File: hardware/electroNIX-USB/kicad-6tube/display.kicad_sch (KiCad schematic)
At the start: 87 parts, among them Q10 MMBTA42, Q11 MMBTA92, Q12 MMBTA42, Q13 MMBTA92, Q14 MMBTA42, Q15 MMBTA92, Q16 MMBTA42, Q17 MMBTA42, Q18 MMBTA42, Q19 MMBTA42, Q20 MMBTA42, Q21 MMBTA42, Q22 MMBTA42, Q23 MMBTA42, Q24 MMBTA42, Q25 MMBTA42, Q26 MMBTA42, Q27 MMBTA42, Q4 MMBTA42, Q5 MMBTA92, Q6 MMBTA42, Q7 MMBTA92, Q8 MMBTA42, Q9 MMBTA92

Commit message: electroNIX-USB: apply RFT Z573M data sheet, add tube footprint
The data book confirms the pinout already in the symbol. The tube is
side-view (not top-view), with 13 flying leads on a 9.53 mm circle and
wire 7 at the front. New footprint electronix:Nixie_RFT_Z573M (top
view, wire 7 toward the front edge) is assigned to the tubes.

Tube current: Ik is 1.5-2.5 mA continuous, 12 mA pulse. PCB-036's 10k
anode resistors averaged only ~0.75 mA per tube when multiplexed. Anode
resistors are now 5k6 (4 tubes) and 3k9 (6 tubes), cathode base
resistors 6k8. To carry the extra HV power, the ladder caps go to
2.2 uF and the 6-tube build uses a 22 uH inductor.

Co-Authored-By: Claude Opus 5.5 <noreply@anthropic.com>
Claude-Session: https://claude.ai/code/session_01AFMfevKEKDGbci8uJGhf4W
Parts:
- N1, N2, N3, N4, N5, N6: footprint (none) -> electronix:Nixie_RFT_Z573M
- R16, R20, R24, R28, R32, R36: value 10k -> 3k9
- R37, R38, R39, R40, R41, R42, R43, R44, R45, R46: value 15k -> 6k8
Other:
- note added: "Pin 4 = internal connection (leave open). Pin 10 = decimal point (unused). Pinout per RFT data book (frank.pocnet.net/sheets/084/z/Z573M.pdf)."
- note added: "Tubes (RFT Z573M side-view, 13 flying leads on 9.53 mm circle, wire 7 at front)"
- note added: "W_n high -> tube n anode at +170V through 3k9: ~7.7 mA peak at 170 V, ~1.3 mA average per tube (Z573M: 1.5-2.5 mA cont., 12 mA pulse). Peak current follows (V_HV - 140 V): keep the firmware HV setpoint <= 180 V. W_5/W_6 = IO12/IO15 (seconds tubes)."
- note removed: "Pin 4 = internal connection (leave open). Pin 10 = PR sign (unused). Pinout from tube-tester.com Z573M page; check against a real tube before layout."
- note removed: "Tubes (RFT Z573M, B13D base, pin 7 at front)"
- note removed: "W_n high -> tube n anode at +170V through 10k. Anode current ~2 mA peak. W_5/W_6 = IO12/IO15 (seconds tubes)."
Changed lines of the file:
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@@
       (justify left top))
 )
-  (text "W_n high -> tube n anode at +170V through 10k. Anode current ~2 mA peak.  W_5/W_6 = IO12/IO15 (seconds tubes)."
-    (at 25 98 0)
+  (text "W_n high -> tube n anode at +170V through 3k9: ~7.7 mA peak at 170 V, ~1.3 mA average per tube (Z573M: 1.5-2.5 mA cont., 12 mA pulse).\nPeak current follows (V_HV - 140 V): keep the firmware HV setpoint <= 180 V.  W_5/W_6 = IO12/IO15 (seconds tubes)."
+    (at 25 95 0)
     (effects
       (font
@@
       (type none))
 )
-  (text "Tubes (RFT Z573M, B13D base, pin 7 at front)"
+  (text "Tubes (RFT Z573M side-view, 13 flying leads on 9.53 mm circle, wire 7 at front)"
     (at 21.27 116.27 0)
     (effects
@@
       (justify left top))
 )
-  (text "Pin 4 = internal connection (leave open). Pin 10 = PR sign (unused).\nPinout from tube-tester.com Z573M page; check against a real tube before layout."
+  (text "Pin 4 = internal connection (leave open). Pin 10 = decimal point (unused).\nPinout per RFT data book (frank.pocnet.net/sheets/084/z/Z573M.pdf)."
     (at 25 195 0)
     (effects
@@
           (size 1.27 1.27))
         (justify left)))
-    (property "Value" "10k"
+    (property "Value" "3k9"
       (at 60.96 77.47 0)
       (effects
@@
           (size 1.27 1.27))
         (justify left)))
-    (property "Value" "10k"
+    (property "Value" "3k9"
       (at 123.19 77.47 0)
       (effects
@@
           (size 1.27 1.27))
         (justify left)))
-    (property "Value" "10k"
+    (property "Value" "3k9"
       (at 185.42 77.47 0)
       (effects
@@
           (size 1.27 1.27))
         (justify left)))
-    (property "Value" "10k"
+    (property "Value" "3k9"
       (at 247.65 77.47 0)
       (effects
@@
           (size 1.27 1.27))
         (justify left)))
-    (property "Value" "10k"
+    (property "Value" "3k9"
       (at 309.88 77.47 0)
       (effects
@@
           (size 1.27 1.27))
         (justify left)))
-    (property "Value" "10k"
+    (property "Value" "3k9"
       (at 370.84 77.47 0)
       (effects
@@
           (size 1.27 1.27))
         (justify left)))
-    (property "Footprint" ""
+    (property "Footprint" "electronix:Nixie_RFT_Z573M"
       (at 59.69 160.02 0)
       (effects
@@
           (size 1.27 1.27))
         (justify left)))
-    (property "Footprint" ""
+    (property "Footprint" "electronix:Nixie_RFT_Z573M"
       (at 121.92 160.02 0)
       (effects
@@
           (size 1.27 1.27))
         (justify left)))
-    (property "Footprint" ""
+    (property "Footprint" "electronix:Nixie_RFT_Z573M"
       (at 184.15 160.02 0)
       (effects
@@
           (size 1.27 1.27))
         (justify left)))
-    (property "Footprint" ""
+    (property "Footprint" "electronix:Nixie_RFT_Z573M"
       (at 246.38 160.02 0)
       (effects
@@
           (size 1.27 1.27))
         (justify left)))
-    (property "Footprint" ""
+    (property "Footprint" "electronix:Nixie_RFT_Z573M"
       (at 308.61 160.02 0)
       (effects
@@
           (size 1.27 1.27))
         (justify left)))
-    (property "Footprint" ""
+    (property "Footprint" "electronix:Nixie_RFT_Z573M"
       (at 369.57 160.02 0)
       (effects
@@
         (font
           (size 1.27 1.27))))
-    (property "Value" "15k"
+    (property "Value" "6k8"
       (at 35.56 273.05 90)
       (effects
@@
         (font
           (size 1.27 1.27))))
-    (property "Value" "15k"
+    (property "Value" "6k8"
       (at 72.39 273.05 90)
       (effects
@@
         (font
           (size 1.27 1.27))))
-    (property "Value" "15k"
+    (property "Value" "6k8"
       (at 107.95 273.05 90)
       (effects
@@
         (font
           (size 1.27 1.27))))
-    (property "Value" "15k"
+    (property "Value" "6k8"
       (at 143.51 273.05 90)
       (effects
@@
         (font
           (size 1.27 1.27))))
-    (property "Value" "15k"
+    (property "Value" "6k8"
       (at 180.34 273.05 90)
       (effects
@@
         (font
           (size 1.27 1.27))))
-    (property "Value" "15k"
+    (property "Value" "6k8"
       (at 215.9 273.05 90)
       (effects
@@
         (font
           (size 1.27 1.27))))
-    (property "Value" "15k"
+    (property "Value" "6k8"
       (at 252.73 273.05 90)
       (effects
@@
         (font
           (size 1.27 1.27))))
-    (property "Value" "15k"
+    (property "Value" "6k8"
       (at 288.29 273.05 90)
       (effects
@@
         (font
           (size 1.27 1.27))))
-    (property "Value" "15k"
+    (property "Value" "6k8"
       (at 323.85 273.05 90)
       (effects
@@
         (font
           (size 1.27 1.27))))
-    (property "Value" "15k"
+    (property "Value" "6k8"
       (at 360.68 273.05 90)
       (effects

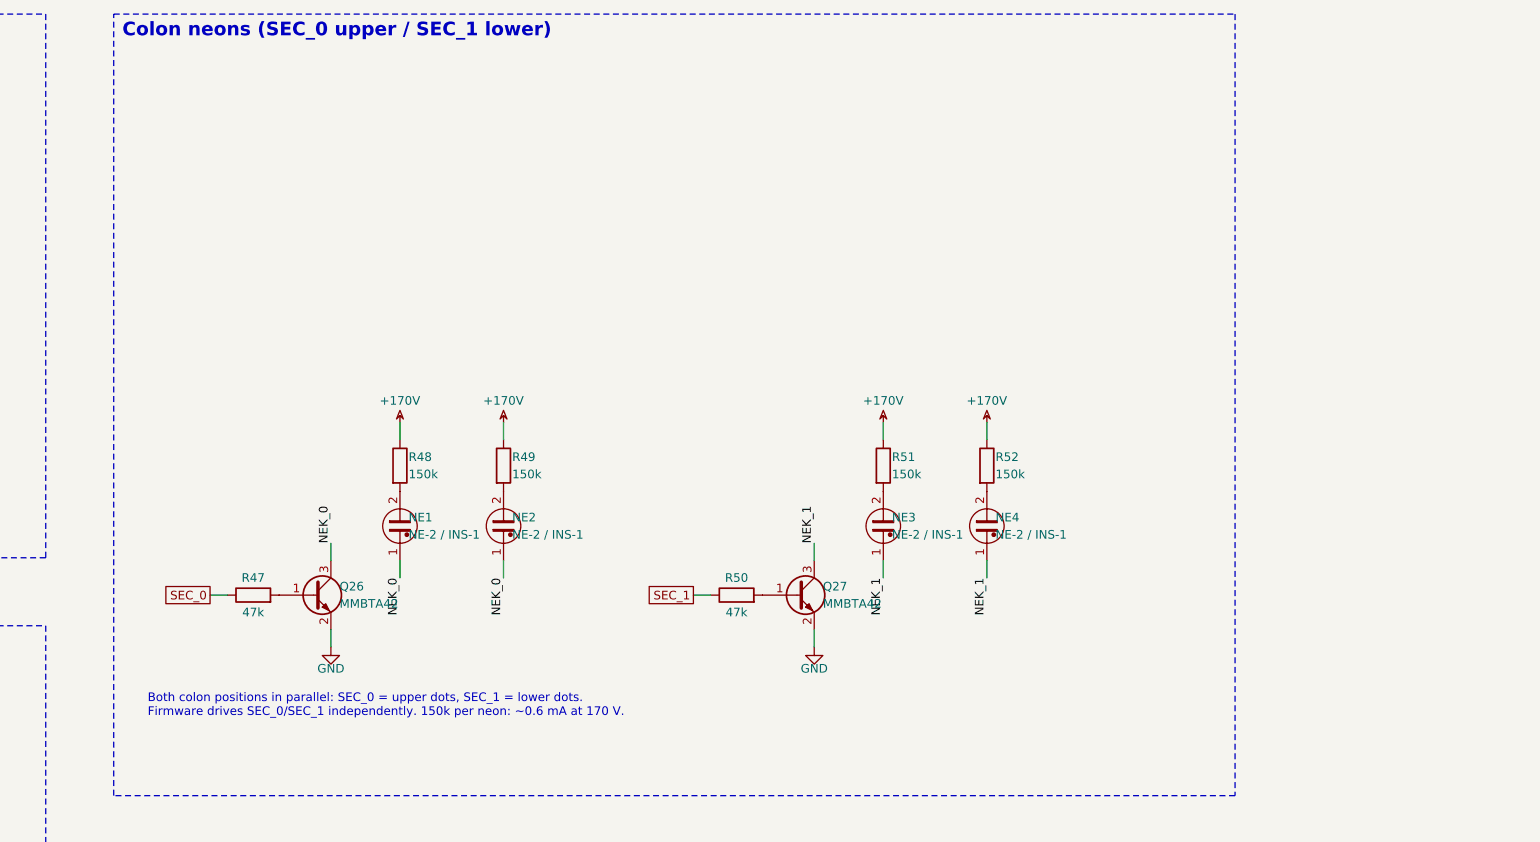
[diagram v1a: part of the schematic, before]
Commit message: electroNIX-USB: socket-adapter footprint, 0.1in neons, 4-tube PCB placement (WIP)
- Z573M socket pins on the electroNIX-2 adapter's 12.6 mm outer ring
  (default footprint), and the direct 9.53 mm footprint resized for the
  1.48 mm socket pins
- Neon_P2.54mm footprint. 6 tubes: HH:MM colon on SEC_0, MM:SS on SEC_1
- SET is a right-angle tact switch; RESET/BOOT use KMR2; low-voltage anode
  resistors moved to 0805
- source/pcb.py: builds the board from the netlist (placement, net
  classes, ESP32 antenna keepout, Freerouting, GND pours, DRC);
  source/fab.sh: fab outputs
- 4-tube board placed (102 x 66 mm, the original kit size), not yet routed

Co-Authored-By: Claude Opus 5.5 <noreply@anthropic.com>
Claude-Session: https://claude.ai/code/session_01AFMfevKEKDGbci8uJGhf4W
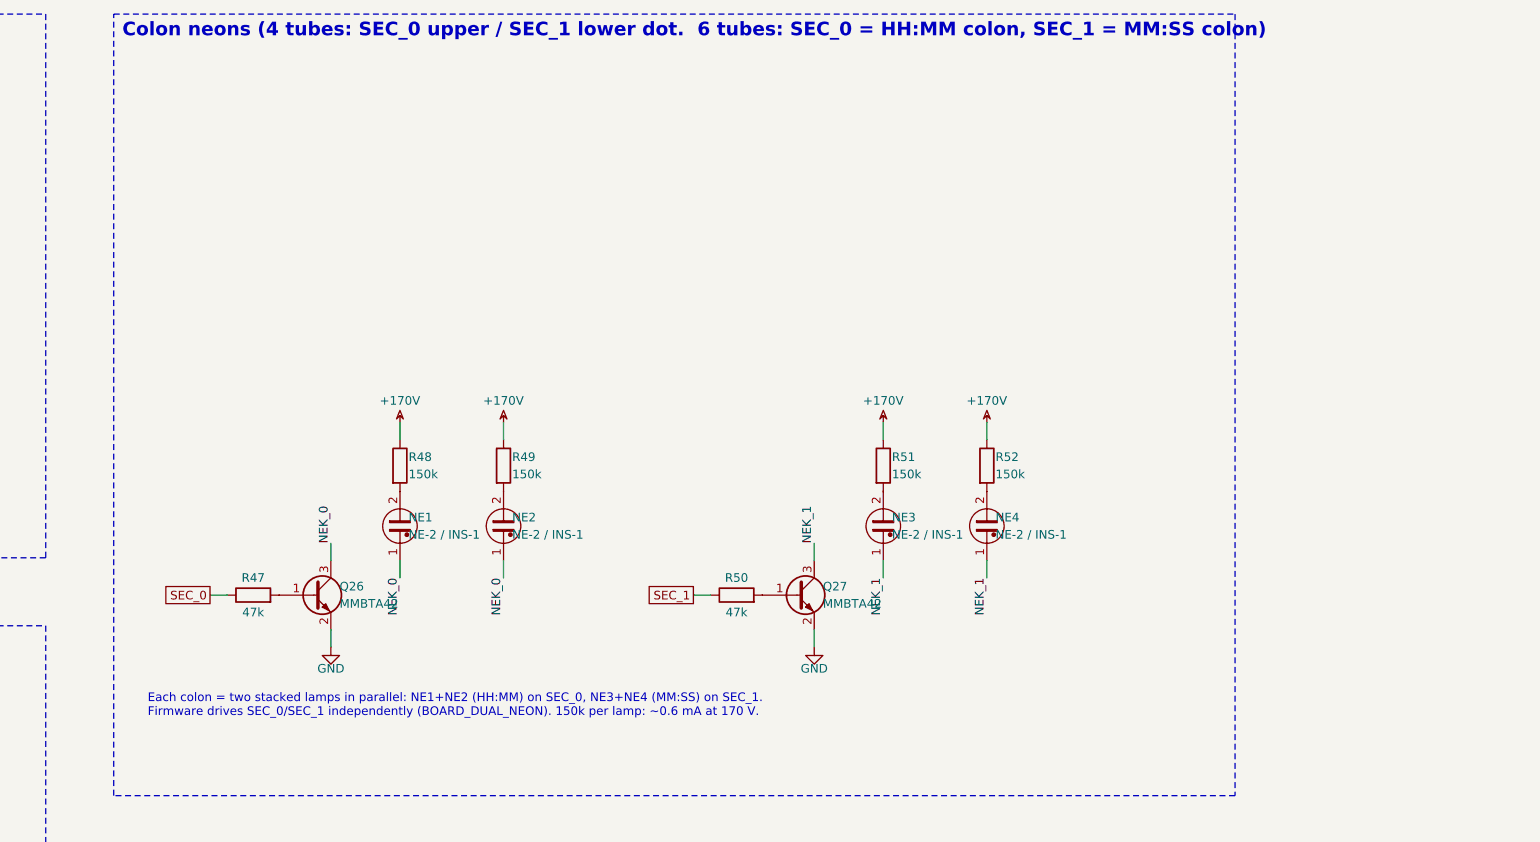
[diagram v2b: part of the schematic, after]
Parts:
- N1, N2, N3, N4, N5, N6: footprint electronix:Nixie_RFT_Z573M -> electronix:Nixie_RFT_Z573M_Adapter
- NE1, NE2, NE3, NE4: footprint (none) -> electronix:Neon_P2.54mm
- R15, R16, R19, R20, R23, R24, R27, R28, R31, R32, R35, R36: footprint Resistor_SMD:R_1206_3216Metric -> Resistor_SMD:R_0805_2012Metric
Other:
- note added: "Colon neons (4 tubes: SEC_0 upper / SEC_1 lower dot. 6 tubes: SEC_0 = HH:MM colon, SEC_1 = MM:SS colon)"
- note added: "Each colon = two stacked lamps in parallel: NE1+NE2 (HH:MM) on SEC_0, NE3+NE4 (MM:SS) on SEC_1. Firmware drives SEC_0/SEC_1 independently (BOARD_DUAL_NEON). 150k per lamp: ~0.6 mA at 170 V."
- note removed: "Both colon positions in parallel: SEC_0 = upper dots, SEC_1 = lower dots. Firmware drives SEC_0/SEC_1 independently. 150k per neon: ~0.6 mA at 170 V."
- note removed: "Colon neons (SEC_0 upper / SEC_1 lower)"
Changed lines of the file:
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@@
       (type none))
 )
-  (text "Colon neons (SEC_0 upper / SEC_1 lower)"
+  (text "Colon neons (4 tubes: SEC_0 upper / SEC_1 lower dot.  6 tubes: SEC_0 = HH:MM colon, SEC_1 = MM:SS colon)"
     (at 411.27 26.27 0)
     (effects
@@
       (justify left top))
 )
-  (text "Both colon positions in parallel: SEC_0 = upper dots, SEC_1 = lower dots.\nFirmware drives SEC_0/SEC_1 independently. 150k per neon: ~0.6 mA at 170 V."
+  (text "Each colon = two stacked lamps in parallel: NE1+NE2 (HH:MM) on SEC_0, NE3+NE4 (MM:SS) on SEC_1.\nFirmware drives SEC_0/SEC_1 independently (BOARD_DUAL_NEON). 150k per lamp: ~0.6 mA at 170 V."
     (at 415 125 0)
     (effects
@@
           (size 1.27 1.27))
         (justify left)))
-    (property "Footprint" "Resistor_SMD:R_1206_3216Metric"
+    (property "Footprint" "Resistor_SMD:R_0805_2012Metric"
       (at 52.07 63.5 0)
       (effects
@@
           (size 1.27 1.27))
         (justify left)))
-    (property "Footprint" "Resistor_SMD:R_1206_3216Metric"
+    (property "Footprint" "Resistor_SMD:R_0805_2012Metric"
       (at 59.69 76.2 0)
       (effects
@@
           (size 1.27 1.27))
         (justify left)))
-    (property "Footprint" "Resistor_SMD:R_1206_3216Metric"
+    (property "Footprint" "Resistor_SMD:R_0805_2012Metric"
       (at 114.3 63.5 0)
       (effects
@@
           (size 1.27 1.27))
         (justify left)))
-    (property "Footprint" "Resistor_SMD:R_1206_3216Metric"
+    (property "Footprint" "Resistor_SMD:R_0805_2012Metric"
       (at 121.92 76.2 0)
       (effects
@@
           (size 1.27 1.27))
         (justify left)))
-    (property "Footprint" "Resistor_SMD:R_1206_3216Metric"
+    (property "Footprint" "Resistor_SMD:R_0805_2012Metric"
       (at 176.53 63.5 0)
       (effects
@@
           (size 1.27 1.27))
         (justify left)))
-    (property "Footprint" "Resistor_SMD:R_1206_3216Metric"
+    (property "Footprint" "Resistor_SMD:R_0805_2012Metric"
       (at 184.15 76.2 0)
       (effects
@@
           (size 1.27 1.27))
         (justify left)))
-    (property "Footprint" "Resistor_SMD:R_1206_3216Metric"
+    (property "Footprint" "Resistor_SMD:R_0805_2012Metric"
       (at 238.76 63.5 0)
       (effects
@@
           (size 1.27 1.27))
         (justify left)))
-    (property "Footprint" "Resistor_SMD:R_1206_3216Metric"
+    (property "Footprint" "Resistor_SMD:R_0805_2012Metric"
       (at 246.38 76.2 0)
       (effects
@@
           (size 1.27 1.27))
         (justify left)))
-    (property "Footprint" "Resistor_SMD:R_1206_3216Metric"
+    (property "Footprint" "Resistor_SMD:R_0805_2012Metric"
       (at 300.99 63.5 0)
       (effects
@@
           (size 1.27 1.27))
         (justify left)))
-    (property "Footprint" "Resistor_SMD:R_1206_3216Metric"
+    (property "Footprint" "Resistor_SMD:R_0805_2012Metric"
       (at 308.61 76.2 0)
       (effects
@@
           (size 1.27 1.27))
         (justify left)))
-    (property "Footprint" "Resistor_SMD:R_1206_3216Metric"
+    (property "Footprint" "Resistor_SMD:R_0805_2012Metric"
       (at 361.95 63.5 0)
       (effects
@@
           (size 1.27 1.27))
         (justify left)))
-    (property "Footprint" "Resistor_SMD:R_1206_3216Metric"
+    (property "Footprint" "Resistor_SMD:R_0805_2012Metric"
       (at 369.57 76.2 0)
       (effects
@@
           (size 1.27 1.27))
         (justify left)))
-    (property "Footprint" "electronix:Nixie_RFT_Z573M"
+    (property "Footprint" "electronix:Nixie_RFT_Z573M_Adapter"
       (at 59.69 160.02 0)
       (effects
@@
           (size 1.27 1.27))
         (justify left)))
-    (property "Footprint" "electronix:Nixie_RFT_Z573M"
+    (property "Footprint" "electronix:Nixie_RFT_Z573M_Adapter"
       (at 121.92 160.02 0)
       (effects
@@
           (size 1.27 1.27))
         (justify left)))
-    (property "Footprint" "electronix:Nixie_RFT_Z573M"
+    (property "Footprint" "electronix:Nixie_RFT_Z573M_Adapter"
       (at 184.15 160.02 0)
       (effects
@@
           (size 1.27 1.27))
         (justify left)))
-    (property "Footprint" "electronix:Nixie_RFT_Z573M"
+    (property "Footprint" "electronix:Nixie_RFT_Z573M_Adapter"
       (at 246.38 160.02 0)
       (effects
@@
           (size 1.27 1.27))
         (justify left)))
-    (property "Footprint" "electronix:Nixie_RFT_Z573M"
+    (property "Footprint" "electronix:Nixie_RFT_Z573M_Adapter"
       (at 308.61 160.02 0)
       (effects
@@
           (size 1.27 1.27))
         (justify left)))
-    (property "Footprint" "electronix:Nixie_RFT_Z573M"
+    (property "Footprint" "electronix:Nixie_RFT_Z573M_Adapter"
       (at 369.57 160.02 0)
       (effects
@@
           (size 1.27 1.27))
         (justify left)))
-    (property "Footprint" ""
+    (property "Footprint" "electronix:Neon_P2.54mm"
       (at 452.12 100.33 0)
       (effects
@@
           (size 1.27 1.27))
         (justify left)))
-    (property "Footprint" ""
+    (property "Footprint" "electronix:Neon_P2.54mm"
       (at 467.36 100.33 0)
       (effects
@@
           (size 1.27 1.27))
         (justify left)))
-    (property "Footprint" ""
+    (property "Footprint" "electronix:Neon_P2.54mm"
       (at 523.24 100.33 0)
       (effects
@@
           (size 1.27 1.27))
         (justify left)))
-    (property "Footprint" ""
+    (property "Footprint" "electronix:Neon_P2.54mm"
       (at 538.48 100.33 0)
       (effects
